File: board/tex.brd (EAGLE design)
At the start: 200 x 100 mm, 248 parts, among them K1 HLS8L-DC5V-S-C, K2 HLS8L-DC5V-S-C, K3 HLS8L-DC5V-S-C, K4 HLS8L-DC5V-S-C, Q47 FDD4141, U14 24LC32A, U15 OPTO-LTV817, U16 OPTO-LTV817, U17 OPTO-LTV817, U18 OPTO-LTV817, U19 RELAY-S108T02PTH, U2 RTC-DS1337S, U20 RELAY-S108T02PTH, U21 IO-HC4051, U5 AZ23C5V1, Y1 32.768KHz

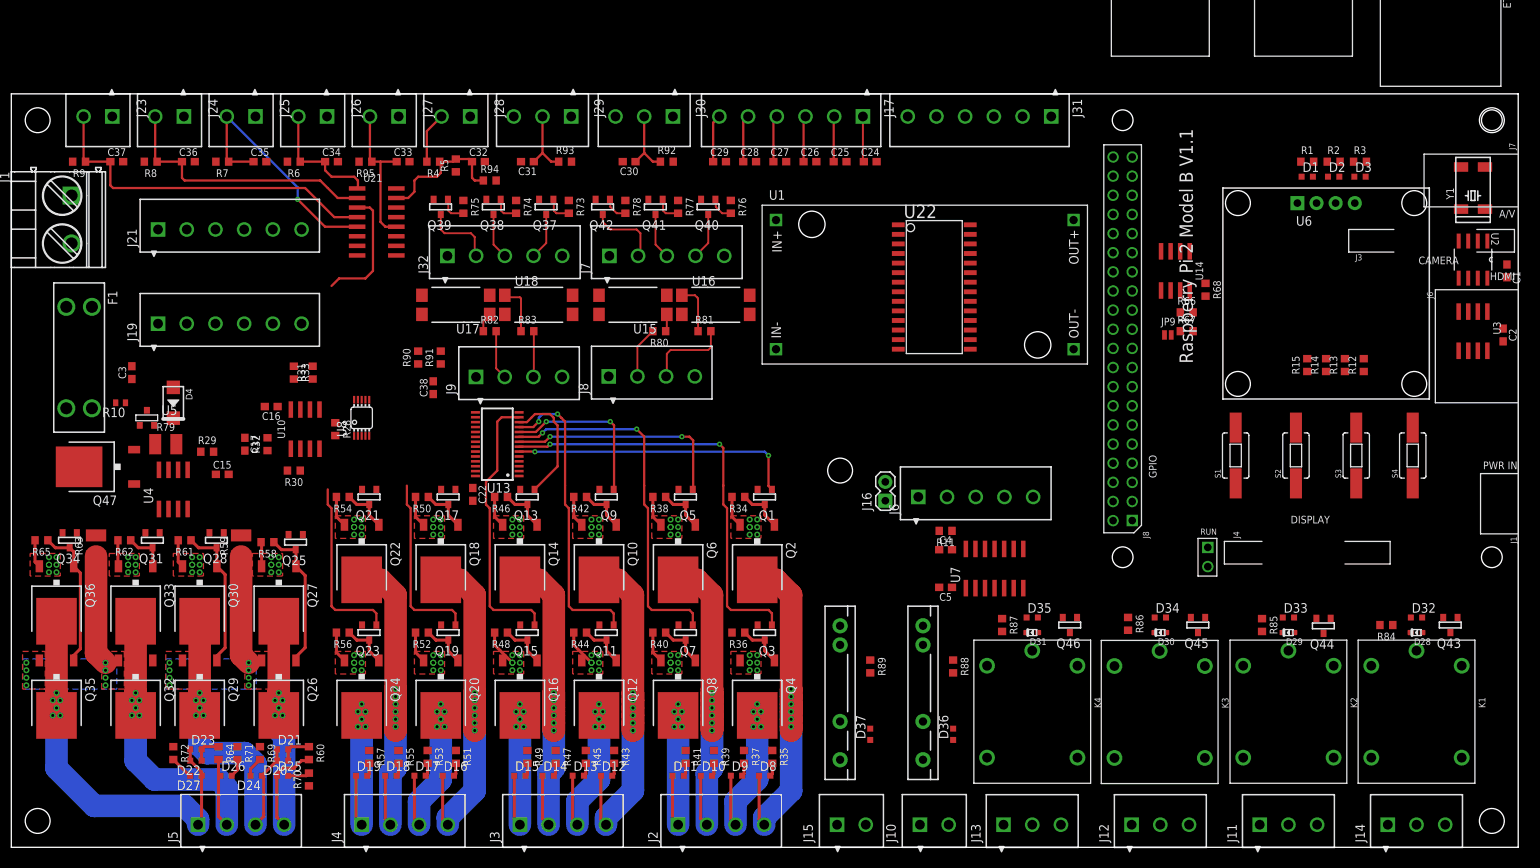
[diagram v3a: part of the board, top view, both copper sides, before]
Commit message: started routing changed rtc to MCP to have vbat
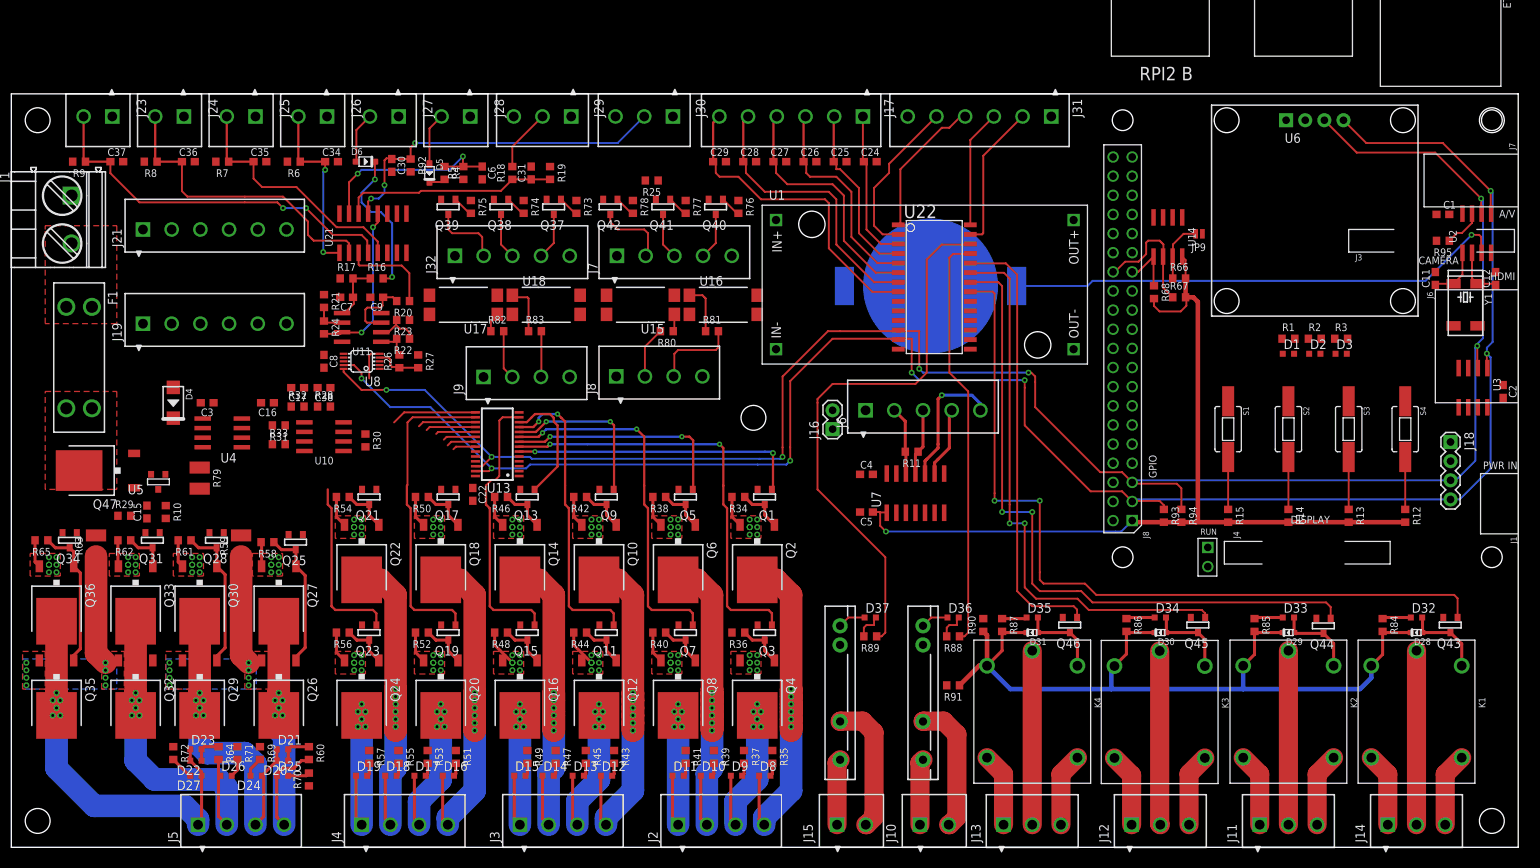
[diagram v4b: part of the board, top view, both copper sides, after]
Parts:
- removed C32, C33: (no value), holla:C0603
- added B1: CONN-COINBATTERYHOLDER-20MM, holla:BAT-HLD-001
- added C11, C12, C8, C9: .1u, holla:C0603
- added C6, C7: (no value), holla:C0603
- added D5, D6: (no value), holla:SOD-323
- added J18: (no value), holla:1X04
- added R16, R17, R18, R19, R25, R26, R27: (no value), holla:R0603
- added R20, R21: 1k, holla:R0603
- added R22: 0, holla:R0603
- added R23: DNP, holla:R0603
- added R24: 10k, holla:R0603
- added U11: (no value), holla:SO08
- R10: device rcl:R0402 -> holla:R0603
- R93, R94, R95: value (none) -> 120
- U2: value RTC-DS1337S -> (none); device holla:SOIC127P600X175-8N -> holla:SO08
- moved R95 143.4 mm to (190.0, 80.5)
- moved R94 102.0 mm to (155.3, 44.0), turned to 270 degrees
- moved R93 92.3 mm to (153.0, 44.0), turned to 270 degrees
- moved R90 83.0 mm to (129.0, 29.5)
- moved R91 80.7 mm to (125.0, 21.5), turned to 180 degrees
- moved R92 34.0 mm to (53.0, 90.5), turned to 270 degrees
- moved C30 31.5 mm to (50.5, 90.5), turned to 270 degrees
- moved D1 23.6 mm to (169.5, 65.5)
- moved D2 23.6 mm to (173.0, 65.5)
- moved D3 23.6 mm to (176.5, 65.5)
- moved R1 23.6 mm to (169.5, 67.5)
- moved R2 23.6 mm to (173.0, 67.5)
- moved R3 23.6 mm to (176.5, 67.5)
- moved R15 22.6 mm to (161.5, 44.0), turned to 270 degrees
- moved R12 20.7 mm to (185.0, 44.0), turned to 270 degrees
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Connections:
- net C_24IN renamed N$194
- removed net !RTC_INTA: U2.3
- removed net !RTC_INTB: U2.7
- removed net N$160: D28.C, D29.C, D30.C, D31.C, K1.2, K2.2, K3.2, K4.2, R85.2, R86.2, R87.2
- new net N$188: R22.2, R26.2, U11.1
- new net N$189: R20.1, U21.3
- new net N$190: R26.1, R27.2, U8.4
- new net N$191: R24.2, U11.7, U21.12
- new net N$192: R95.1, U2.7
- new net N$20: D5.A, J28.2
- new net N$25: D6.C, R16.2
- new net N$26: D6.A, J27.2
- new net N$27: J29.2, R18.2
- new net N$28: U8.2
- new net N$38: R22.1, R23.2, U11.2
- new net N$39: R21.2, R24.1, U11.6
- new net N$55: C9.1, R20.2, U11.3
- net +3V3: now also R93.2, R94.2
- net +5V: now also J18.2; no longer R6.2, R7.2, R8.2, R9.2, R92.2, R93.2, R94.2, U21.16
- net AGND: now also C15.2, C16.2, C17.2, C30.2, C31.2, C34.2, C35.2, C36.2, C37.2, C38.2, C6.2, C7.2, C8.2, C9.2, J23.1, J24.1, J25.1, J26.1, J27.1, J28.1, J29.1, J30.1, R17.1, R19.1, R21.1, R23.1, R25.2, R27.1, R5.1, U10.4, U11.4, U21.6, U21.7, U21.8, U8.3
- net AVCC: now also C8.1, R6.2, R7.2, R8.2, R9.2, R92.2, U11.8, U21.16
- net GND: now also B1.-, C11.2, C12.2, J18.1, R10.2, R25.1; no longer C15.2, C16.2, C17.2, C30.2, C31.2, C32.2, C33.2, C34.2, C35.2, C36.2, C37.2, C38.2, J23.1, J24.1, J25.1, J26.1, J27.1, J28.1, J29.1, J30.1, R10.1, R5.1, U10.4, U2.4, U21.6, U21.7, U21.8, U8.3
- net N$118: now also B1.+1, U2.3; no longer U21.3, U8.4
- net N$124: now also R18.1, R19.2; no longer J29.2, R93.1
- net N$130: now also C6.1; no longer C32.1, R94.1
- net N$138: now also C7.1, R16.1, R17.2, U11.5; no longer C33.1, J27.2, R95.1, U21.12
- net N$172: now also D28.C, D29.C, D30.C, D31.C, K1.2, K2.2, K3.2, K4.2, R85.2, R86.2, R87.2
- net N$2: now also D5.C; no longer J28.2
- net N$3: now also C11.1
- net N$4: now also R10.1; no longer R10.2
- net N$5: now also C12.1
- net N$61: now also Q34.1
- net SCL: now also J18.3, R94.1
- net SDA: now also J18.4, R93.1
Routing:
- net SDA: track 0.00 -> 262.4 mm, vias 0 -> 7
- net SCL: track 0.00 -> 261.4 mm, vias 0 -> 7
- net +3V3: track 0.00 -> 118.2 mm, vias 0 -> 1
- net RELAY0EN: track 0.00 -> 106.3 mm, vias 0 -> 2
- net N$172: track 0.00 -> 105.8 mm
- net RELAY1EN: track 0.00 -> 90.3 mm, vias 0 -> 2
- net RELAY2EN: track 0.00 -> 74.5 mm, vias 0 -> 2
- net RELAY5EN: track 0.00 -> 73.7 mm
- net RELAY3EN: track 0.00 -> 58.9 mm
- net RELAY4EN: track 0.00 -> 55.2 mm
- net N$118: track 16.6 -> 66.7 mm, vias 0 -> 1
- net N$120: track 9.10 -> 46.4 mm, vias 0 -> 3
- net N$114: track 6.34 -> 42.3 mm
- net N$111: track 6.26 -> 37.6 mm
- net N$109: track 6.18 -> 33.0 mm
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- added copper zone on layer 1, net N$101
- added copper zone on layer 1, net N$194

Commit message: routing
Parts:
- removed D3: (no value), holla:LED0603
- removed R14, R15, R3: (no value), holla:R0603
- removed S2, S4: (no value), holla:TACTILE-SWITCH-6MMX3.5MM
- added D0: (no value), holla:LED0603
- added R0: (no value), holla:R0603
- moved R25 35.4 mm to (57.6, 66.1)
- moved S1 23.5 mm to (185.0, 55.5)
- moved D1 3.50 mm to (173.0, 65.5)
- moved D2 3.50 mm to (176.5, 65.5)
- moved R1 3.50 mm to (173.0, 67.5)
- moved R2 3.50 mm to (176.5, 67.5)
- turned C4 to 180 degrees
- renumbered S3 to S0
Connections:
- removed net DCMOTOR1ENCA: U15.4
- removed net DCMOTOR1ENCB: U16.4
- removed net DCMOTOR2ENCA: U17.4
- removed net DCMOTOR2ENCB: U18.4
- removed net N$10: U7.5
- removed net N$106: PCB1.P$7
- removed net N$11: U7.2
- removed net N$110: PCB1.P$12
- removed net N$112: PCB1.P$16
- removed net N$113: PCB1.P$18
- removed net N$115: PCB1.P$22
- removed net N$116: PCB1.P$24
- removed net N$117: PCB1.P$26
- removed net N$119: PCB1.P$32
- removed net N$12: U7.4
- removed net N$121: PCB1.P$36
- removed net N$122: PCB1.P$38
- removed net N$123: PCB1.P$40
- removed net N$125: PCB1.P$37
- removed net N$126: PCB1.P$35
- removed net N$127: PCB1.P$33
- removed net N$128: PCB1.P$31
- removed net N$129: PCB1.P$29
- removed net N$131: PCB1.P$23
- removed net N$132: PCB1.P$21
- removed net N$133: PCB1.P$19
- removed net N$134: PCB1.P$17
- removed net N$135: PCB1.P$15
- removed net N$136: PCB1.P$13
- removed net N$137: PCB1.P$11
- removed net N$19: U7.3
- removed net N$21: R15.1, S1.P$2
- removed net N$22: R14.1, S2.P$2
- removed net N$23: R13.1, S0.P$2
- removed net N$24: R12.1, S4.P$2
- removed net N$28: U8.2
- removed net N$31 (its old number): D3.A, R3.1
- removed net N$32: R1.2
- removed net N$33: R2.2
- removed net N$34: R3.2
- removed net STEPPER1DIR: Q38.1, R74.2
- removed net STEPPER1EN: Q37.1, R73.2
- removed net STEPPER1STEP: Q39.1, R75.2
- removed net STEPPER2DIR: Q41.1, R77.2
- removed net STEPPER2EN: Q40.1, R76.2
- removed net STEPPER2STEP: Q42.1, R78.2
- new net ADCALERT: PCB1.P$13, U8.2
- new net D0: PCB1.P$21, R0.2
- new net D1: PCB1.P$23, R1.2
- new net D2: PCB1.P$24, R2.2
- new net DCMOTORAENCA: PCB1.P$18, U15.4
- new net DCMOTORAENCB: PCB1.P$16, U16.4
- new net DCMOTORBENCA: PCB1.P$26, U17.4
- new net DCMOTORBENCB: PCB1.P$22, U18.4
- new net N$29: D0.A, R0.1
- new net RXEN: PCB1.P$12, U7.4
- new net S0: PCB1.P$15, R13.1, S0.P$2
- new net S1: PCB1.P$19, R12.1, S1.P$2
- new net STEPPERADIR: PCB1.P$32, Q41.1, R77.2
- new net STEPPERAEN: PCB1.P$29, Q40.1, R76.2
- new net STEPPERASTEP: PCB1.P$31, Q42.1, R78.2
- new net STEPPERBDIR: PCB1.P$36, Q38.1, R74.2
- new net STEPPERBEN: PCB1.P$33, Q37.1, R73.2
- new net STEPPERBSTEP: PCB1.P$35, Q39.1, R75.2
- new net TXEN: PCB1.P$7, U7.3
- net +3V3: now also PCB1.P$17; no longer R14.2, R15.2
- net GND: now also D0.C; no longer D3.C, S2.P$1, S4.P$1
- net INPUTINTERRUPT: now also PCB1.P$11
- net SENSORS0: now also PCB1.P$40
- net SENSORS1: now also PCB1.P$37
- net SENSORS2: now also PCB1.P$38
- net UART0_RX: now also U7.2
- net UART0_TX: now also U7.5
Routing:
- net DCMOTORBENCA: track 0.00 -> 111.7 mm, vias 0 -> 2
- net ADCALERT: track 0.00 -> 104.7 mm, vias 0 -> 4
- net SENSORS1: track 0.00 -> 104.6 mm, vias 0 -> 1
- net SENSORS0: track 0.00 -> 103.2 mm, vias 0 -> 1
- net SENSORS2: track 0.00 -> 100.0 mm, vias 0 -> 1
- net STEPPERBSTEP: track 0.00 -> 98.8 mm, vias 0 -> 1
- net DCMOTORAENCA: track 0.00 -> 92.0 mm, vias 0 -> 4
- net DCMOTORBENCB: track 0.00 -> 91.2 mm, vias 0 -> 2
- net STEPPERBDIR: track 0.00 -> 88.5 mm, vias 0 -> 1
- net STEPPERBEN: track 0.00 -> 83.5 mm, vias 0 -> 1
- net STEPPERASTEP: track 0.00 -> 77.7 mm, vias 0 -> 1
- net STEPPERADIR: track 0.00 -> 70.7 mm, vias 0 -> 2
- net STEPPERAEN: track 0.00 -> 65.0 mm, vias 0 -> 2
- net DCMOTORAENCB: track 0.00 -> 53.0 mm, vias 0 -> 2
- net S1: track 0.00 -> 49.2 mm, vias 0 -> 1
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
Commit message: routing complete
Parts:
- added C10: (no value), holla:C0603
- added R3: (no value), holla:R0603
- moved C15 22.3 mm to (39.4, 50.8), turned to 180 degrees
- moved R10 8.56 mm to (11.9, 44.5), turned to 180 degrees
- moved C16 7.60 mm to (35.6, 51.6)
- moved R28 5.10 mm to (46.5, 57.4), turned to 270 degrees
- moved C38 2.48 mm to (43.2, 59.2), turned to 90 degrees
- moved R25 1.98 mm to (56.3, 67.7)
- moved D4 1.97 mm to (19.6, 58.7), turned to 0 degrees
- moved U5 1.44 mm to (18.3, 49.3)
- moved C2 1.25 mm to (198.0, 59.2), turned to 90 degrees
- moved R31 1.03 mm to (34.5, 56.4), turned to 270 degrees
- moved R29 0.87 mm to (15.7, 44.5)
- moved R79 0.87 mm to (24.1, 49.0)
- moved R36 0.79 mm to (96.8, 27.8)
- moved R40 0.79 mm to (86.2, 27.8)
- moved R44 0.79 mm to (75.8, 27.8)
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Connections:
- net +5V: now also R3.1; no longer C38.1, U8.8
- net AGND: now also C10.2, U8.1
- net AVCC: now also C10.1, C38.1, R3.2, U8.8
- net GND: no longer U8.1
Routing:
- net VBATT: track 61.3 -> 229.6 mm, vias 112 -> 129
- net N$61: track 3.07 -> 61.0 mm, vias 0 -> 2
- net +5V: track 0.00 -> 48.8 mm, vias 0 -> 10
- net N$62: track 3.89 -> 51.8 mm, vias 0 -> 2
- net AVCC: track 0.00 -> 43.6 mm, vias 0 -> 11
- net N$87: track 4.35 -> 43.9 mm, vias 0 -> 2
- net N$97: track 0.00 -> 36.6 mm
- net GND: track 0.00 -> 30.5 mm, vias 0 -> 3
- net N$88: track 5.32 -> 35.3 mm, vias 0 -> 2
- net MOTORB_SENSE: track 14.5 -> 38.0 mm, vias 8 -> 10
- net SDA: track 262.8 -> 285.0 mm, vias 7 -> 10
- net N$91: track 30.2 -> 50.5 mm, vias 0 -> 2
- net +3V3: track 106.7 -> 126.8 mm
- net SCL: track 261.7 -> 280.7 mm, vias 7 -> 9
- net ADC0_2: track 0.00 -> 18.2 mm
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- added copper zone on layer 16, net +5V
- added copper zone on layer 1, net AGND
- added copper zone on layer 16, net AVCC
- added copper zone on layer 1, net GND
- added copper zone on layer 16, net VBATT
- added copper zone on layer 1, net VBATTISENSE

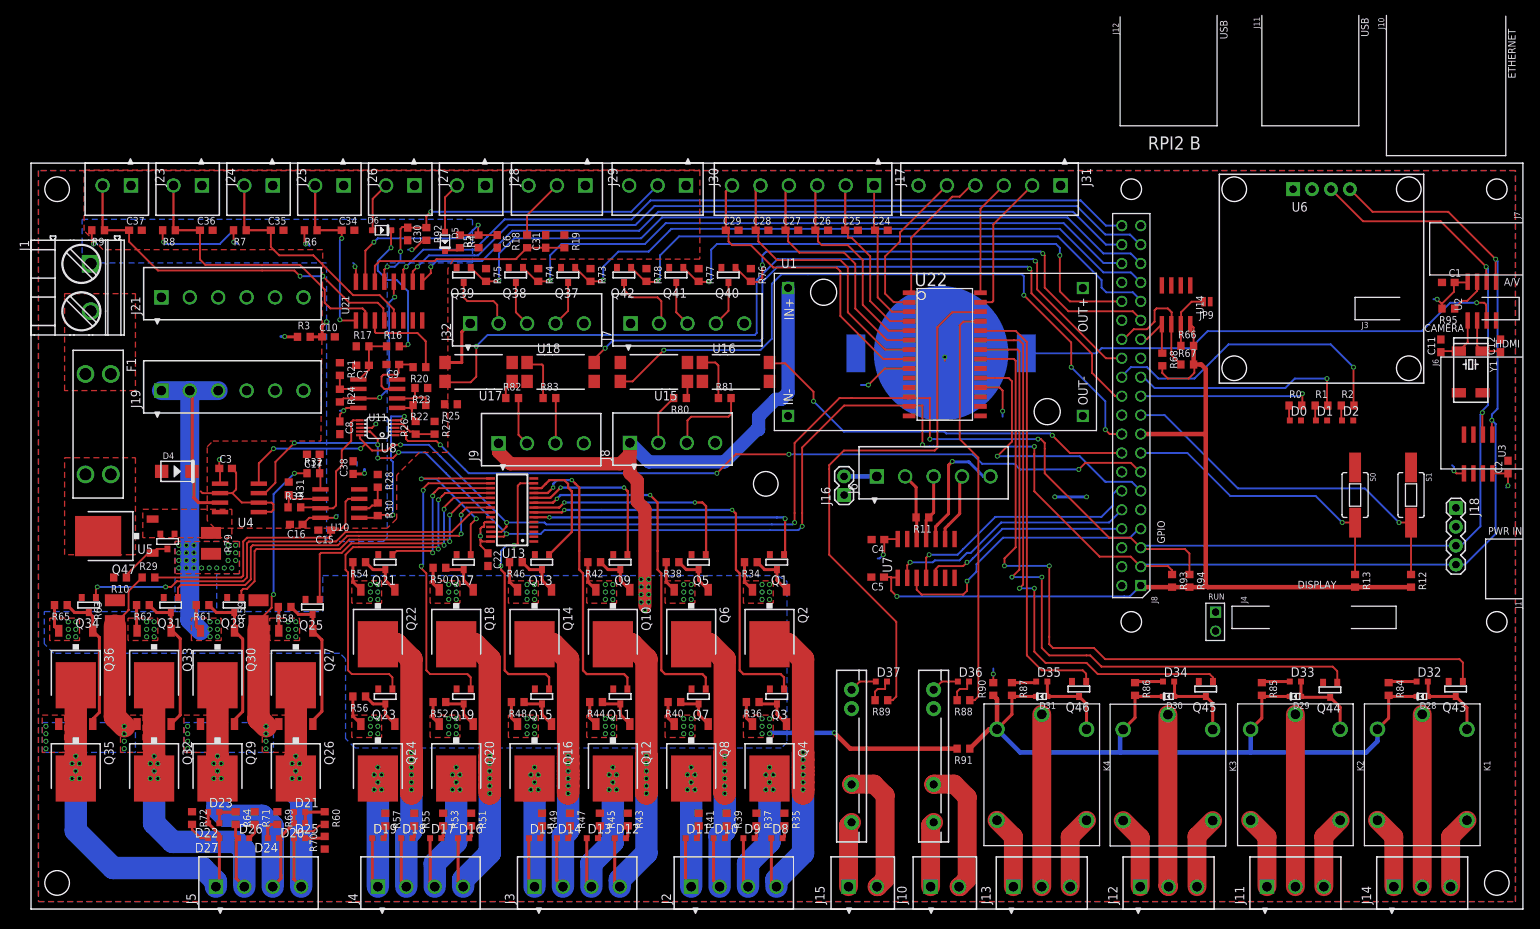
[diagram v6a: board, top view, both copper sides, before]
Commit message: ready to place names
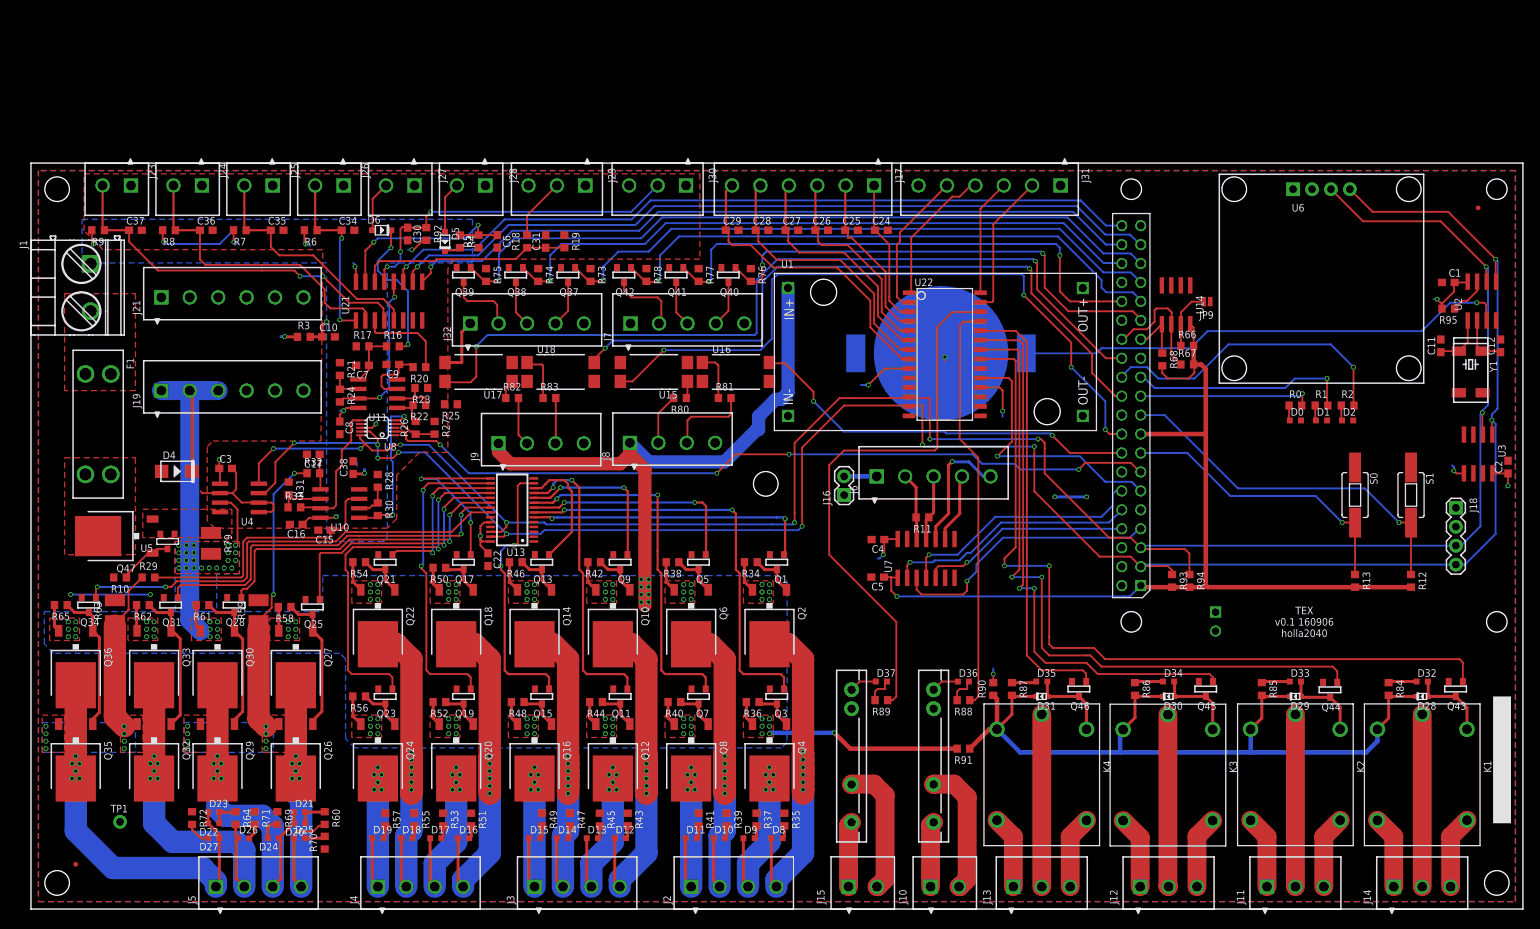
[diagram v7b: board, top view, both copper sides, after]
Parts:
- added JP1, JP2: FIDUCIALUFIDUCIAL, holla:MICRO-FIDUCIAL
- added TP1: (no value), holla:TPTHRU
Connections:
- removed net ADC0_3: U8.7
- net AGND: now also U8.7
- net GND: now also TP1.1, U2.4
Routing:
- net GND: track 30.5 -> 41.2 mm, vias 3 -> 5
- net N$7: track 21.6 -> 19.7 mm
- net N$114: track 42.3 -> 40.8 mm
- net N$109: track 33.0 -> 31.8 mm
- net N$111: track 37.6 -> 36.5 mm
- net VBATT: track 229.6 -> 228.6 mm
- net N$108: track 28.4 -> 27.5 mm
- net N$103: track 23.5 -> 22.8 mm
- net N$102: track 20.2 -> 19.6 mm
- net N$54: track 24.0 -> 23.4 mm
- net N$49: track 48.0 -> 48.6 mm
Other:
- board text added: "TEX v0.1 160906 holla2040"
